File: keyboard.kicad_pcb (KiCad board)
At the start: 2 copper layers, 112 x 91.3 mm, 27 parts, among them SW1 SW_PUSH, SW10 SW_PUSH, SW15 SW_PUSH, SW16 SW_PUSH, SW17 SW_PUSH, SW18 SW_PUSH, SW2 SW_PUSH, SW23 SW_PUSH, SW24 SW_PUSH, SW25 SW_PUSH, SW26 SW_PUSH, SW3 SW_PUSH, SW30 SW_PUSH, SW31 SW_PUSH, SW32 SW_PUSH, SW33 SW_PUSH, SW8 SW_PUSH, SW9 SW_PUSH

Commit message: Update PCB
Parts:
- removed YJB1: YJ14015, keyboard:YJ-14015
- added SW15: SW_PUSH, keyboard:MX_ALPS_PG1350_noLed, F.Cu at (126.0, 29.0)
- added SW16: SW_PUSH, keyboard:MX_ALPS_PG1350_noLed, F.Cu at (106.7, 40.4)
- added SW17: SW_PUSH, keyboard:MX_ALPS_PG1350_noLed, F.Cu at (145.0, 26.0)
- added SW18: SW_PUSH, keyboard:MX_ALPS_PG1350_noLed, F.Cu at (84.1, 39.9)
- added SW23: SW_PUSH, keyboard:MX_ALPS_PG1350_noLed, F.Cu at (164.2, 25.4)
- added SW24: SW_PUSH, keyboard:MX_ALPS_PG1350_noLed, F.Cu at (84.8, 61.5)
- added SW25: SW_PUSH, keyboard:MX_ALPS_PG1350_noLed, F.Cu at (183.4, 25.4)
- added SW26: SW_PUSH, keyboard:MX_ALPS_PG1350_noLed, F.Cu at (84.8, 82.0)
- added YJT2: YJ14015, keyboard:YJ-14015, B.Cu at (201.6, 78.0)
- moved SW10 70.6 mm to (84.6, 102.6)
- moved YJT1 0.20 mm to (201.6, 77.9)
- renumbered SW18 to SW10, SW23 to SW11, SW24 to SW12, SW25 to SW13, SW26 to SW14, SW30 to SW19, SW31 to SW20, SW32 to SW21, SW33 to SW22, SW8 to SW4, SW9 to SW5, SW10 to SW6, SW15 to SW7, SW16 to SW8, SW17 to SW9
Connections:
- SW1 pad 2: SW00L -> SW01L
- SW10 pad 2: SW32L -> SW10L
- SW11 pad 2: SW03L -> SW11L
- SW12 pad 2: SW13L -> SW12L
- SW13 pad 2: SW23L -> SW13L
- SW14 pad 2: SW33L -> SW14L
- SW19 pad 2: SW04L -> SW19L
- SW2 pad 2: SW10L -> SW02L
- SW20 pad 2: SW14L -> SW20L
- SW21 pad 2: SW24L -> SW21L
- SW22 pad 2: SW34L -> SW22L
- SW3 pad 2: SW20L -> SW03L
- SW4 pad 2: SW01L -> SW04L
- SW5 pad 2: SW11L -> SW05L
- SW6 pad 2: SW21L -> SW06L
- SW7 pad 2: SW02L -> SW07L
- SW8 pad 2: SW12L -> SW08L
- SW9 pad 2: SW22L -> SW09L
- YJT1 pad 10: SW00L -> SW26L
- YJT1 pad 22: SW24L -> SW08L
- YJT1 pad 23: SW32L -> SW07L
- YJT1 pad 24: SW33L -> SW06L
- YJT1 pad 25: Net-(YJT1-Pad25) -> SW15L
- YJT1 pad 26: Net-(YJT1-Pad26) -> SW09L
- YJT1 pad 27: SW34L -> SW05L
- YJT1 pad 28: Net-(YJT1-Pad28) -> SW16L
- YJT1 pad 29: Net-(YJT1-Pad29) -> SW17L
- YJT1 pad 30: Net-(YJT1-Pad30) -> SW18L
- YJT1 pad 33: Net-(YJT1-Pad33) -> SW19L
- YJT1 pad 34: Net-(YJT1-Pad34) -> SW24L
- YJT1 pad 35: Net-(YJT1-Pad35) -> SW25L
- YJT1 pad 36: Net-(YJT1-Pad36) -> unconnected-(YJT1-P20-Pad36)
- YJT1 pad 5: Net-(YJT1-Pad5) -> unconnected-(YJT1-P24-Pad5)
- YJT1 pad 6: Net-(YJT1-Pad6) -> unconnected-(YJT1-P25-Pad6)
- YJT1 pad 7: Net-(YJT1-Pad7) -> unconnected-(YJT1-NC-Pad7)
- YJT1 pad 8: Net-(YJT1-Pad8) -> unconnected-(YJT1-NC-Pad8)
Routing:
- net VCC: track 153.8 -> 0.00 mm, vias 3 -> 0
- net SW20L: track 120.4 -> 0.00 mm, vias 1 -> 0
- net DIOL: track 117.7 -> 0.00 mm, vias 1 -> 0
- net CLKL: track 117.3 -> 0.00 mm, vias 1 -> 0
- net SW10L: track 104.0 -> 0.00 mm, vias 1 -> 0
- net SW00L: track 100.5 -> 0.00 mm, vias 1 -> 0
- net SW21L: track 93.2 -> 0.00 mm, vias 1 -> 0
- net SW01L: track 90.0 -> 0.00 mm, vias 1 -> 0
- net SW11L: track 87.0 -> 0.00 mm, vias 1 -> 0
- net SW32L: track 76.9 -> 0.00 mm, vias 1 -> 0
- net SW22L: track 73.7 -> 0.00 mm, vias 1 -> 0
- net SW12L: track 68.6 -> 0.00 mm, vias 1 -> 0
- net SW02L: track 68.5 -> 0.00 mm, vias 1 -> 0
- net SW33L: track 58.8 -> 0.00 mm, vias 1 -> 0
- net SW34L: track 55.2 -> 0.00 mm, vias 1 -> 0
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- removed copper zone on B.Cu, net GND
- removed copper zone on F.Cu, net GND
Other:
- board outline removed

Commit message: Approximate layout
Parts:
- moved SW26 128.3 mm to (203.0, 132.0), turned to -30 degrees
- moved SW24 103.4 mm to (180.0, 102.0)
- moved SW25 98.8 mm to (183.2, 124.2), turned to -15 degrees
- moved Ref** 85.9 mm to (143.0, 139.0)
- moved SW18 81.9 mm to (162.0, 65.0)
- moved SW4 76.2 mm to (90.0, 115.0)
- moved Ref** 72.0 mm to (137.0, 139.0)
- moved SW16 66.1 mm to (144.0, 95.0)
- moved Ref** 63.1 mm to (155.0, 139.0)
- moved SW7 61.7 mm to (108.0, 95.0)
- moved SW23 61.6 mm to (180.0, 85.0)
- moved SW8 60.1 mm to (108.0, 112.0)
- moved SW14 57.3 mm to (144.0, 61.0), turned to 0 degrees
- moved SW10 56.0 mm to (126.0, 65.0)
- moved SW15 52.2 mm to (144.0, 78.0)
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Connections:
- YJT1 pad 10: SW26L -> SW17L
- YJT1 pad 13: SW14L -> SW21L
- YJT1 pad 14: SW13L -> SW02L
- YJT1 pad 15: SW12L -> SW06L
- YJT1 pad 16: SW11L -> SW10L
- YJT1 pad 17: SW10L -> SW14L
- YJT1 pad 18: SW20L -> SW18L
- YJT1 pad 19: SW21L -> SW22L
- YJT1 pad 2: SW04L -> SW01L
- YJT1 pad 20: SW22L -> SW03L
- YJT1 pad 21: SW23L -> SW07L
- YJT1 pad 22: SW08L -> SW11L
- YJT1 pad 23: SW07L -> SW15L
- YJT1 pad 24: SW06L -> SW19L
- YJT1 pad 25: SW15L -> SW23L
- YJT1 pad 26: SW09L -> SW04L
- YJT1 pad 27: SW05L -> SW08L
- YJT1 pad 28: SW16L -> SW12L
- YJT1 pad 29: SW17L -> SW16L
- YJT1 pad 3: SW03L -> SW05L
- YJT1 pad 30: SW18L -> SW20L
- YJT1 pad 33: SW19L -> SW24L
- YJT1 pad 34: SW24L -> SW25L
- YJT1 pad 35: SW25L -> SW26L
- YJT1 pad 4: SW02L -> SW09L
- YJT1 pad 9: SW01L -> SW13L
- YJT2 pad 10: SW26L -> SW08L
- YJT2 pad 13: SW14L -> SW19L
- YJT2 pad 14: SW13L -> SW15L
- YJT2 pad 15: SW12L -> SW11L
- YJT2 pad 16: SW11L -> SW07L
- YJT2 pad 17: SW10L -> SW03L
- YJT2 pad 18: SW20L -> SW22L
- YJT2 pad 19: SW21L -> SW18L
- YJT2 pad 2: SW04L -> SW26L
- YJT2 pad 20: SW22L -> SW14L
- YJT2 pad 21: SW23L -> SW10L
- YJT2 pad 22: SW08L -> SW06L
- YJT2 pad 23: SW07L -> SW02L
- YJT2 pad 24: SW06L -> SW21L
- YJT2 pad 25: SW15L -> SW23L
- YJT2 pad 26: SW09L -> SW04L
- YJT2 pad 27: SW05L -> SW17L
- YJT2 pad 28: SW16L -> SW13L
- YJT2 pad 29: SW17L -> SW16L
- YJT2 pad 3: SW03L -> SW25L
- YJT2 pad 30: SW18L -> SW20L
- YJT2 pad 33: SW19L -> SW09L
- YJT2 pad 34: SW24L -> SW05L
- YJT2 pad 35: SW25L -> SW01L
- YJT2 pad 4: SW02L -> SW24L
- YJT2 pad 9: SW01L -> SW12L
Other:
- board text removed: "<text>"
- board text removed: "keyboard"

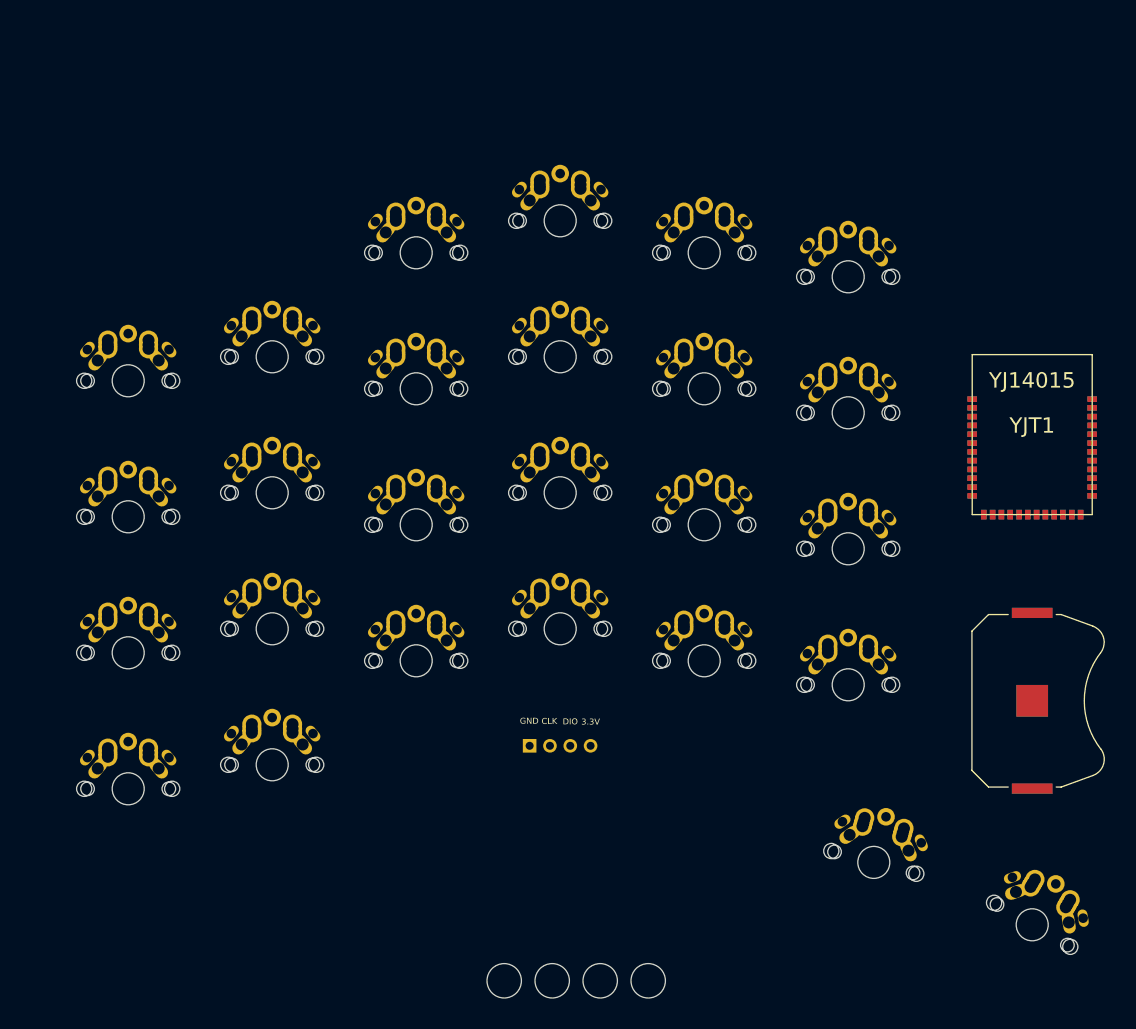
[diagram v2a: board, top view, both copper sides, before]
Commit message: Adjust spacing and stagger, add splitkb tenting puck
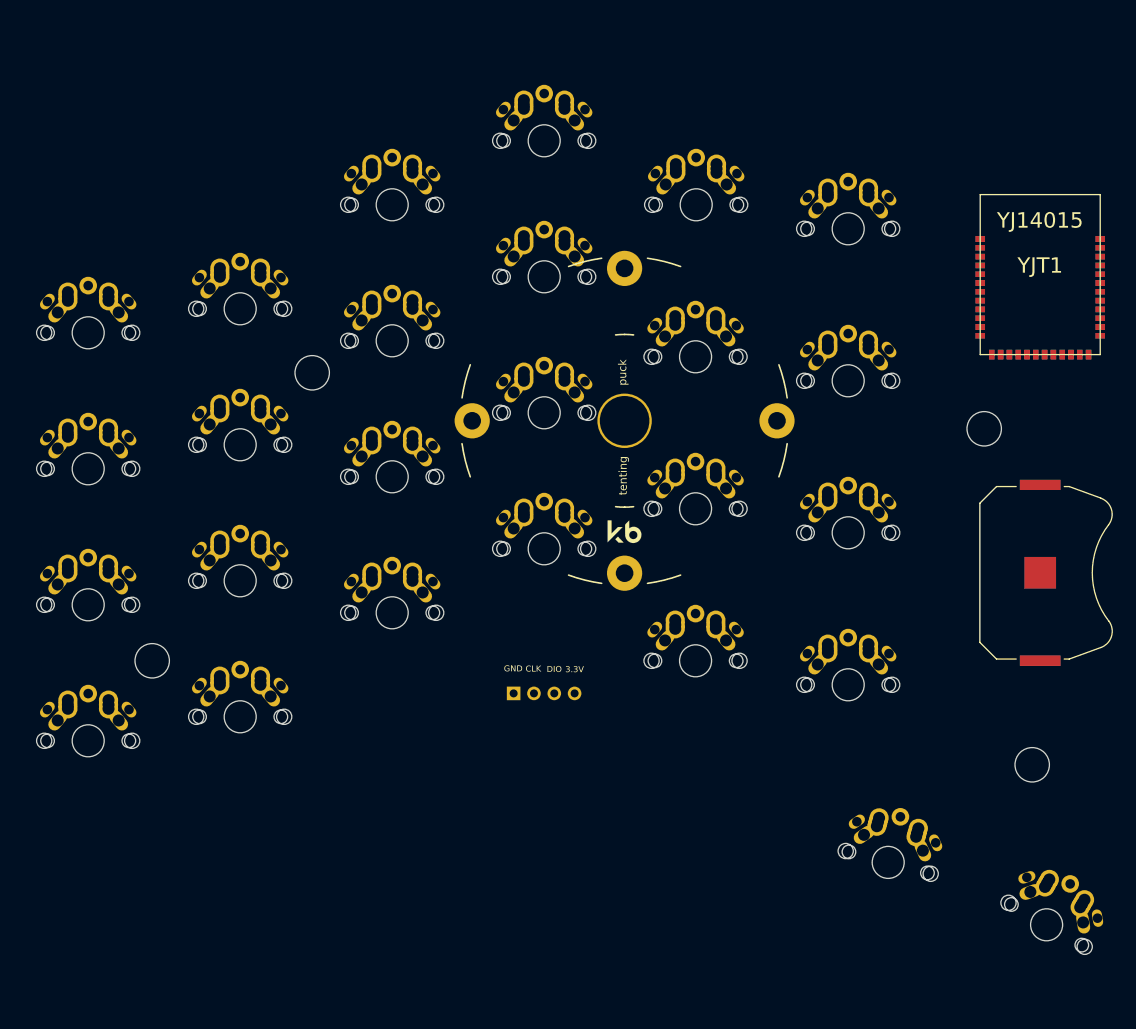
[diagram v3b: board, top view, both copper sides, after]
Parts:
- added H1: MountingHole_Pad, keyboard:Tenting_Puck, F.Cu at (152.1, 69.0)
- moved Ref** 84.1 mm to (197.0, 70.0)
- moved Ref** 79.7 mm to (113.0, 63.0)
- moved Ref** 64.0 mm to (93.0, 99.0)
- moved Ref** 55.1 mm to (203.0, 112.0)
- moved YJT1 20.0 mm to (204.0, 60.7)
- moved YJT2 20.0 mm to (204.0, 60.7)
- moved BT1 16.0 mm to (204.0, 88.0)
- moved BT2 16.0 mm to (204.0, 88.0)
- moved SW13 10.2 mm to (142.0, 34.0)
- moved SW14 10.2 mm to (142.0, 51.0)
- moved SW15 10.2 mm to (142.0, 68.0)
- moved SW16 10.2 mm to (142.0, 85.0)
- moved SW1 7.81 mm to (85.0, 58.0)
- moved SW2 7.81 mm to (85.0, 75.0)
- moved SW3 7.81 mm to (85.0, 92.0)
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
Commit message: Add board outline
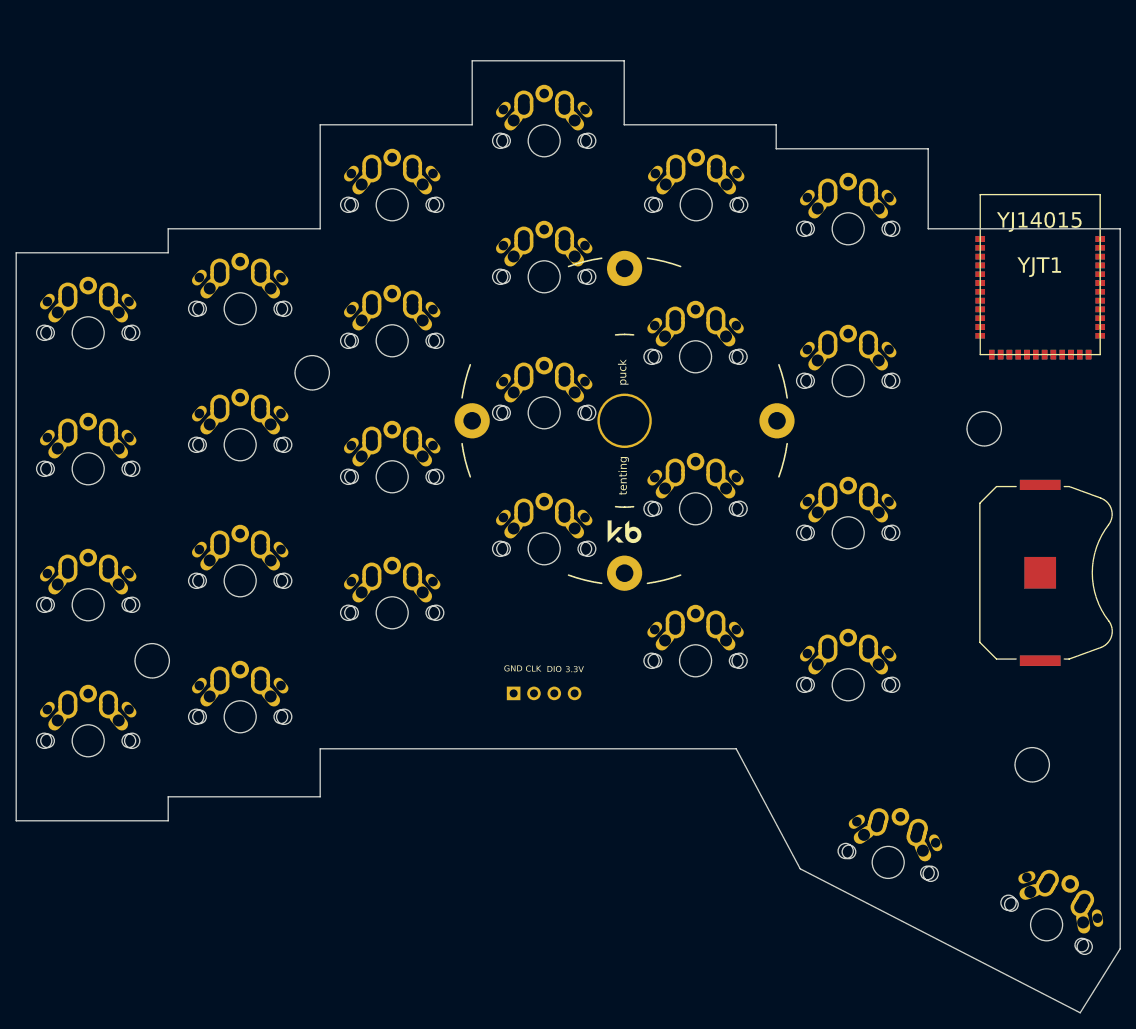
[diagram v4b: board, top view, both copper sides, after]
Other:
- board outline added: 138 x 119 mm
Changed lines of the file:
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@@
       (net 40 "unconnected-(YJT2-P20-Pad36)") (pinfunction "P20") (pintype "bidirectional+no_connect"))
   )
+  (gr_poly
+    (pts
+      (xy 152 32)
+      (xy 171 32)
+      (xy 171 35)
+      (xy 190 35)
+      (xy 190 45)
+      (xy 214 45)
+      (xy 214 135)
+      (xy 209 143)
+      (xy 174 125)
+      (xy 166 110)
+      (xy 114 110)
+      (xy 114 116)
+      (xy 95 116)
+      (xy 95 119)
+      (xy 76 119)
+      (xy 76 48)
+      (xy 95 48)
+      (xy 95 45)
+      (xy 114 45)
+      (xy 114 32)
+      (xy 133 32)
+      (xy 133 24)
+      (xy 152 24)
+    )
+    (stroke (width 0.05) (type solid)) (fill none) (layer "Edge.Cuts"))
   (gr_text "3.3V" (at 145.8 100.0762) (layer "B.SilkS")
     (effects (font (size 0.75 0.75) (thickness 0.1875)) (justify mirror))

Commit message: set trace / spacing, 4 layers
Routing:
- added copper zone on In1.Cu, net GND
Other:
- copper layers 2 -> 4
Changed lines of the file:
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@@
   (layers
     (0 "F.Cu" signal)
+    (1 "In1.Cu" signal)
+    (2 "In2.Cu" signal)
     (31 "B.Cu" signal)
     (32 "B.Adhes" user "B.Adhesive")
@@
       (layer "F.Mask" (type "Top Solder Mask") (thickness 0.01))
       (layer "F.Cu" (type "copper") (thickness 0.035))
-      (layer "dielectric 1" (type "core") (thickness 1.51) (material "FR4") (epsilon_r 4.5) (loss_tangent 0.02))
+      (layer "dielectric 1" (type "prepreg") (thickness 0.1) (material "FR4") (epsilon_r 4.5) (loss_tangent 0.02))
+      (layer "In1.Cu" (type "copper") (thickness 0.035))
+      (layer "dielectric 2" (type "core") (thickness 1.24) (material "FR4") (epsilon_r 4.5) (loss_tangent 0.02))
+      (layer "In2.Cu" (type "copper") (thickness 0.035))
+      (layer "dielectric 3" (type "prepreg") (thickness 0.1) (material "FR4") (epsilon_r 4.5) (loss_tangent 0.02))
       (layer "B.Cu" (type "copper") (thickness 0.035))
       (layer "B.Mask" (type "Bottom Solder Mask") (thickness 0.01))
@@
     (effects (font (size 0.75 0.75) (thickness 0.1875)))
   )
+  (zone (net 18) (net_name "GND") (layer "In1.Cu") (hatch edge 0.5)
+    (connect_pads (clearance 0.508))
+    (min_thickness 0.25) (filled_areas_thickness no)
+    (fill yes (thermal_gap 0.5) (thermal_bridge_width 0.5))
+    (polygon
+      (pts
+        (xy 70 20)
+        (xy 220 20)
+        (xy 220 149)
+        (xy 70 149)
+      )
+    )
+  )
 )

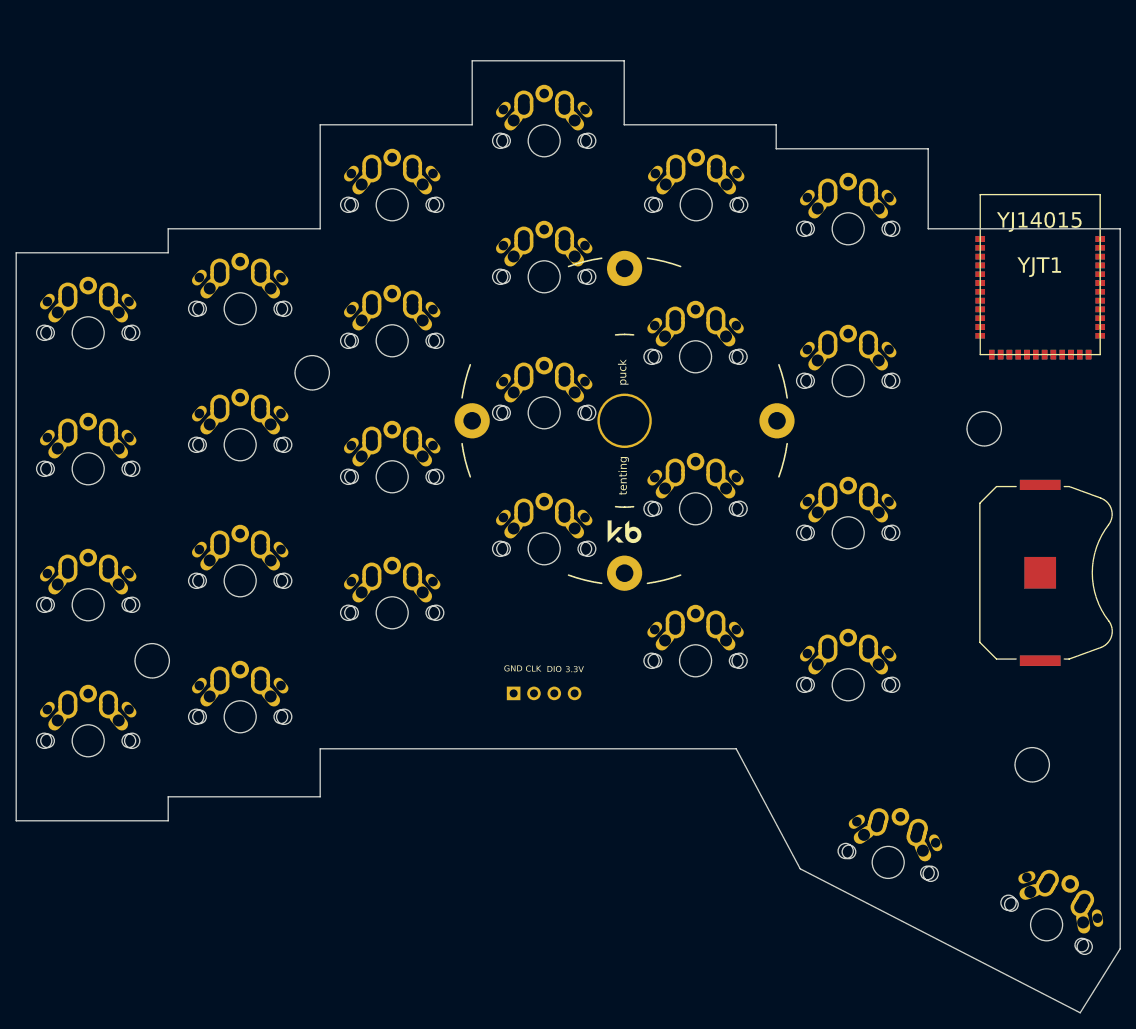
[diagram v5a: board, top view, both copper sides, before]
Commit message: fix spacing, add a mod key
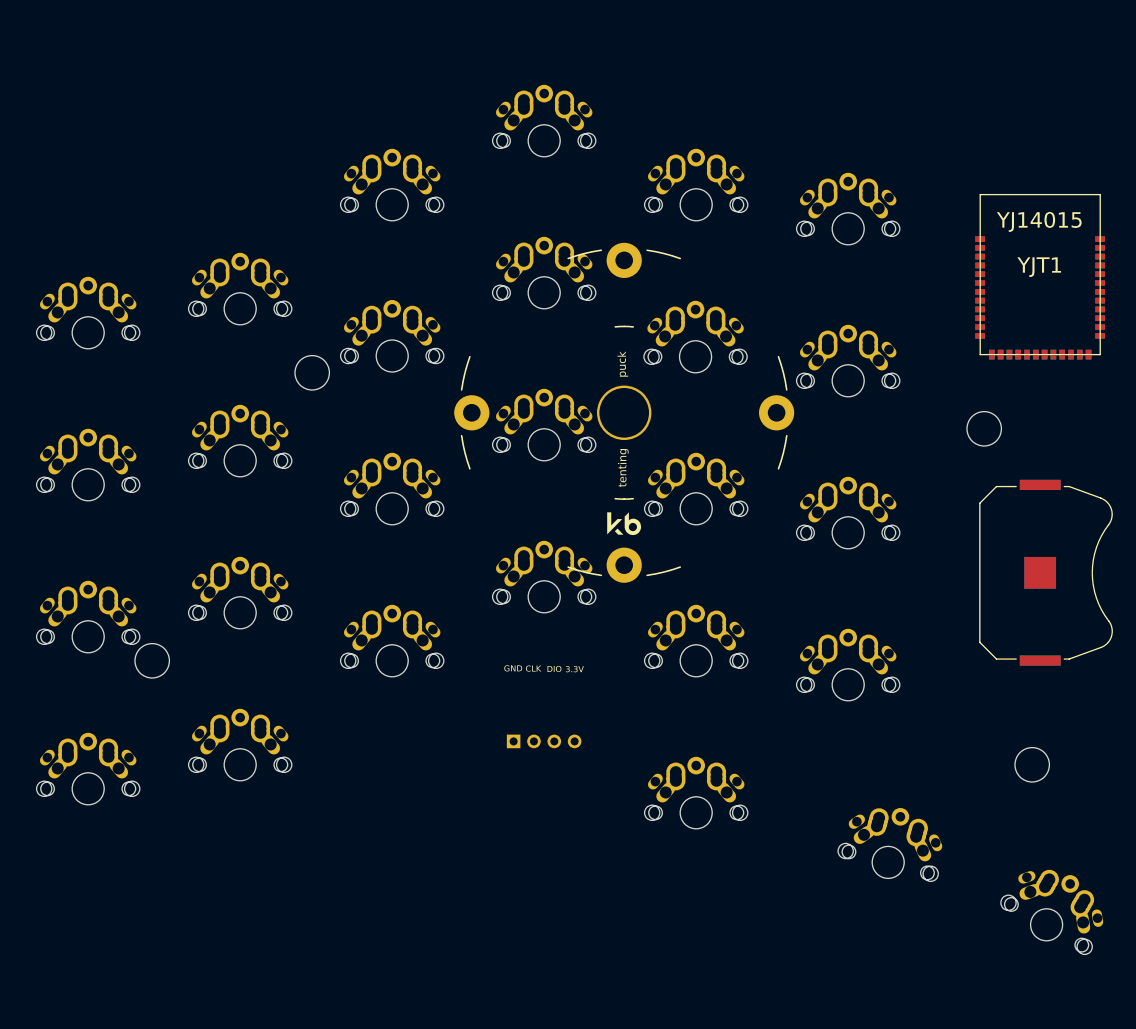
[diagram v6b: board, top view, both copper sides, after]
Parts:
- added SW27: SW_PUSH, keyboard:MX_ALPS_PG1350_noLed, F.Cu at (161.0, 118.0)
- moved PROGL1 6.00 mm to (145.8, 109.1)
- moved SW12 6.00 mm to (123.0, 99.0)
- moved SW16 6.00 mm to (142.0, 91.0)
- moved SW4 6.00 mm to (85.0, 115.0)
- moved SW8 6.00 mm to (104.0, 112.0)
- moved SW11 4.00 mm to (123.0, 80.0)
- moved SW15 4.00 mm to (142.0, 72.0)
- moved SW3 4.00 mm to (85.0, 96.0)
- moved SW7 4.00 mm to (104.0, 93.0)
- moved SW14 2.00 mm to (142.0, 53.0)
- moved SW2 2.00 mm to (85.0, 77.0)
- moved SW6 2.00 mm to (104.0, 74.0)
- moved SW10 1.90 mm to (123.0, 60.9)
- moved H1 1.00 mm to (152.0, 68.0)
- moved SW19 0.08 mm to (161.0, 80.0)
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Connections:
- YJT1 pad 5: unconnected-(YJT1-P24-Pad5) -> SW27L
- YJT2 pad 10: SW08L -> SW17L
- YJT2 pad 13: SW19L -> SW21L
- YJT2 pad 14: SW15L -> SW02L
- YJT2 pad 15: SW11L -> SW06L
- YJT2 pad 16: SW07L -> SW10L
- YJT2 pad 17: SW03L -> SW14L
- YJT2 pad 18: SW22L -> SW18L
- YJT2 pad 19: SW18L -> SW22L
- YJT2 pad 2: SW26L -> SW01L
- YJT2 pad 20: SW14L -> SW03L
- YJT2 pad 21: SW10L -> SW07L
- YJT2 pad 22: SW06L -> SW11L
- YJT2 pad 23: SW02L -> SW15L
- YJT2 pad 24: SW21L -> SW19L
- YJT2 pad 27: SW17L -> SW08L
- YJT2 pad 28: SW13L -> SW12L
- YJT2 pad 3: SW25L -> SW05L
- YJT2 pad 33: SW09L -> SW24L
- YJT2 pad 34: SW05L -> SW25L
- YJT2 pad 35: SW01L -> SW26L
- YJT2 pad 4: SW24L -> SW09L
- YJT2 pad 5: unconnected-(YJT2-P24-Pad5) -> SW27L
- YJT2 pad 9: SW12L -> SW13L
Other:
- board outline removed
